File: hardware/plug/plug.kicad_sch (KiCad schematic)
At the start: 37 parts, among them J101 Cortex, J102 DX07S016JA3, SW101 SKSG, SW102 SKSG, SW103 SKSG, SW104 SKSG, SW105 SKSG, U101 ATSAMD51J, U102 TPS78433QWDRBRQ1, Y101 32k768

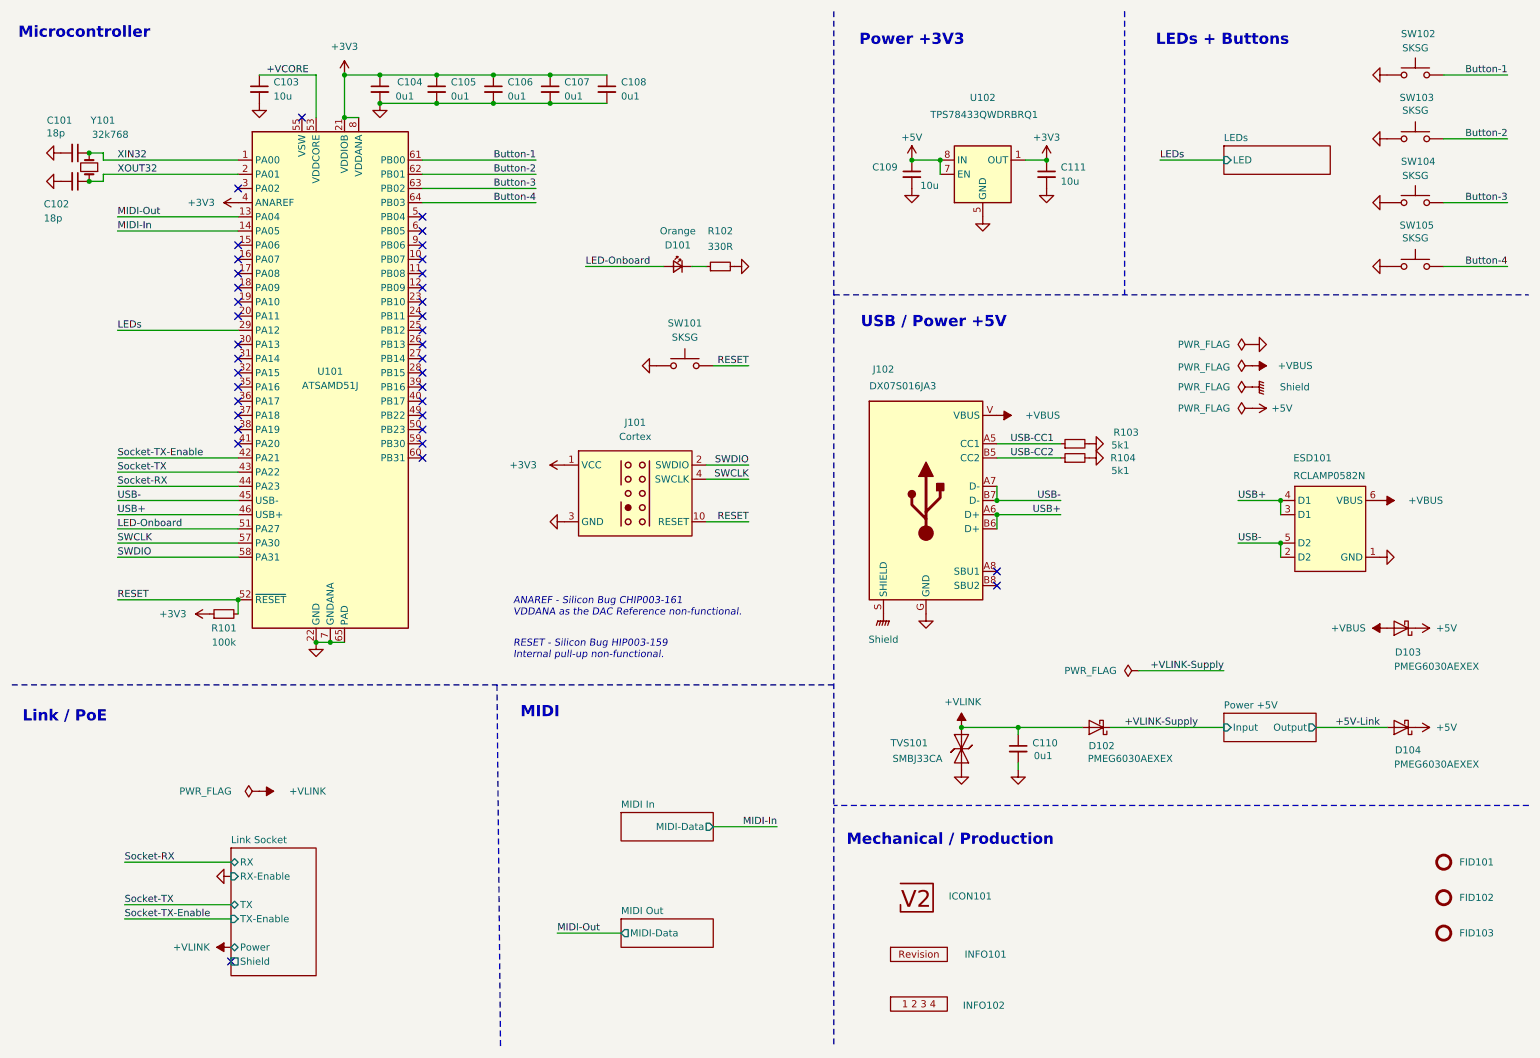
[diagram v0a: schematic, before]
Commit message: Split into socket and plug
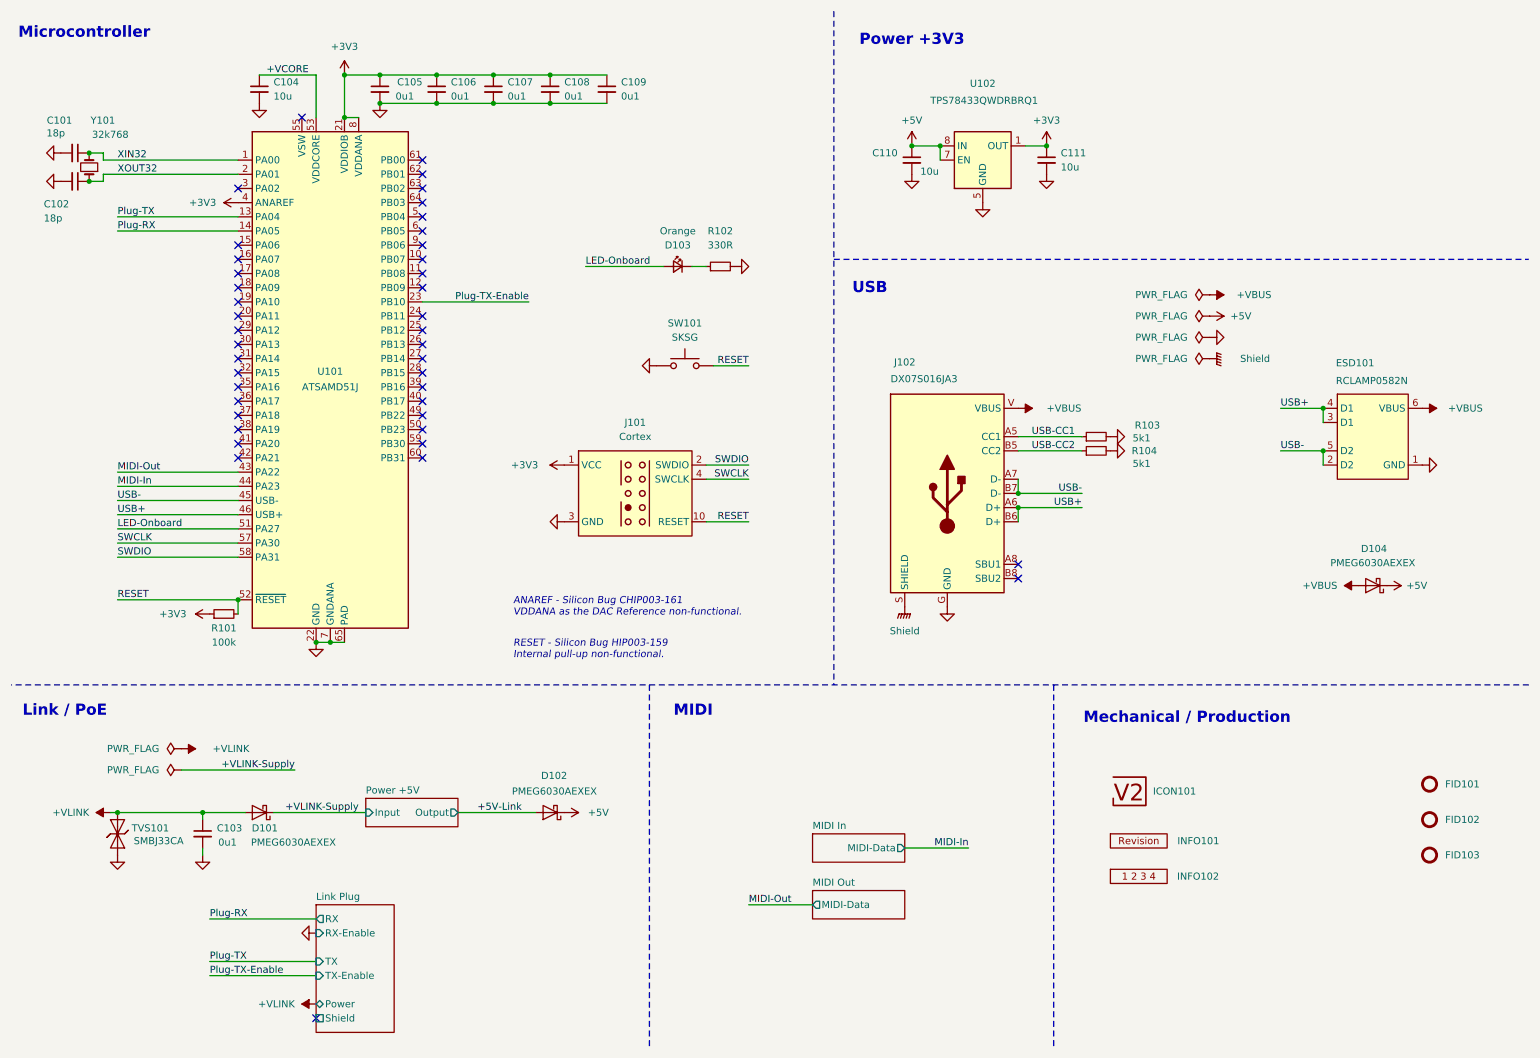
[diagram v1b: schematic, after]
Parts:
- removed SW102, SW103, SW104, SW105: SKSG, V2_Button_Switch_SMD:SKSG, symbol V2_Switch:SKSG
- renumbered C110 to C103, C103 to C104, C104 to C105, C105 to C106, C106 to C107, C107 to C108, C108 to C109, C109 to C110, D102 to D101, D104 to D102, D101 to D103, D103 to D104
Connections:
- net Socket-RX is gone; now on net MIDI-In: U101.44 (PA23)
- net Socket-TX is gone; now on net MIDI-Out: U101.43 (PA22)
- net MIDI-In: no longer U101.14 (PA05)
- net MIDI-Out: no longer U101.13 (PA04)
- net Plug-TX-Enable: now reaches U101.23 (PB10)
- net Button-1: no longer names the net of U101.61 (PB00)
- net Button-2: no longer names the net of U101.62 (PB01)
- net Button-3: no longer names the net of U101.63 (PB02)
- net Button-4: no longer names the net of U101.64 (PB03)
- net LEDs: no longer names the net of U101.29 (PA12)
- net Socket-TX-Enable: no longer names the net of U101.42 (PA21)
- new net Plug-RX: U101.14 (PA05)
- new net Plug-TX: U101.13 (PA04)
- no-connect marks 37 -> 42
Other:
- removed sheet LEDs
- removed sheet Link Socket
- added sheet Link Plug (LinkPlug.kicad_sch)
- note added: "USB"
- note removed: "LEDs + Buttons"
- note removed: "USB / Power +5V"
- title: V2 connect -> V2 connect-plug
- moved on the sheet: C103, C110, C111, D101, D102, D104, ESD101, FID101, FID102, FID103, ICON101, INFO101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

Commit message: Good Bye Imperial
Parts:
- C101, C102: footprint V2_Capacitor_SMD:C_0603 -> V2_Capacitor_SMD:C_1608; symbol V2_Capacitor:0603_18p -> V2_Capacitor:1608_18p
- C103, C105, C106, C107, C108, C109: footprint V2_Capacitor_SMD:C_0603 -> V2_Capacitor_SMD:C_1608; symbol V2_Capacitor:0603_0u1 -> V2_Capacitor:1608_0u1
- C104: footprint V2_Capacitor_SMD:C_0603 -> V2_Capacitor_SMD:C_1608; symbol V2_Capacitor:0603_10u -> V2_Capacitor:1608_10u
- C110, C111: footprint V2_Capacitor_SMD:C_0805 -> V2_Capacitor_SMD:C_2012; symbol V2_Capacitor:0805_10u -> V2_Capacitor:2012_10u
- D103: footprint V2_LED:LED_0603 -> V2_LED:LED_1608; symbol V2_LED:0603_Orange -> V2_LED:1608_Orange
- R101: footprint V2_Resistor_SMD:R_0603 -> V2_Resistor_SMD:R_1608; symbol V2_Resistor:0603_100k -> V2_Resistor:1608_100k
- R102: footprint V2_Resistor_SMD:R_0603 -> V2_Resistor_SMD:R_1608; symbol V2_Resistor:0603_330R -> V2_Resistor:1608_330R
- R103, R104: footprint V2_Resistor_SMD:R_0603 -> V2_Resistor_SMD:R_1608; symbol V2_Resistor:0603_5k1 -> V2_Resistor:1608_5k1

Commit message: Refresh
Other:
- moved on the sheet: D101, D102

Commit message: Refresh
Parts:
- INFO102: value Layer_Numbers -> Layer_Numbers-4; footprint V2_Production:Layer_Numbers -> V2_Production:Layer_Numbers-4; symbol V2_Production:Layer_Numbers -> V2_Production:Layer_Numbers-4
